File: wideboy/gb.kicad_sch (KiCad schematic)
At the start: 13 parts, among them U12 CPU-AGB, U13 SRAM-AGB, Y1 4.194304M, Y1A 4.194304M

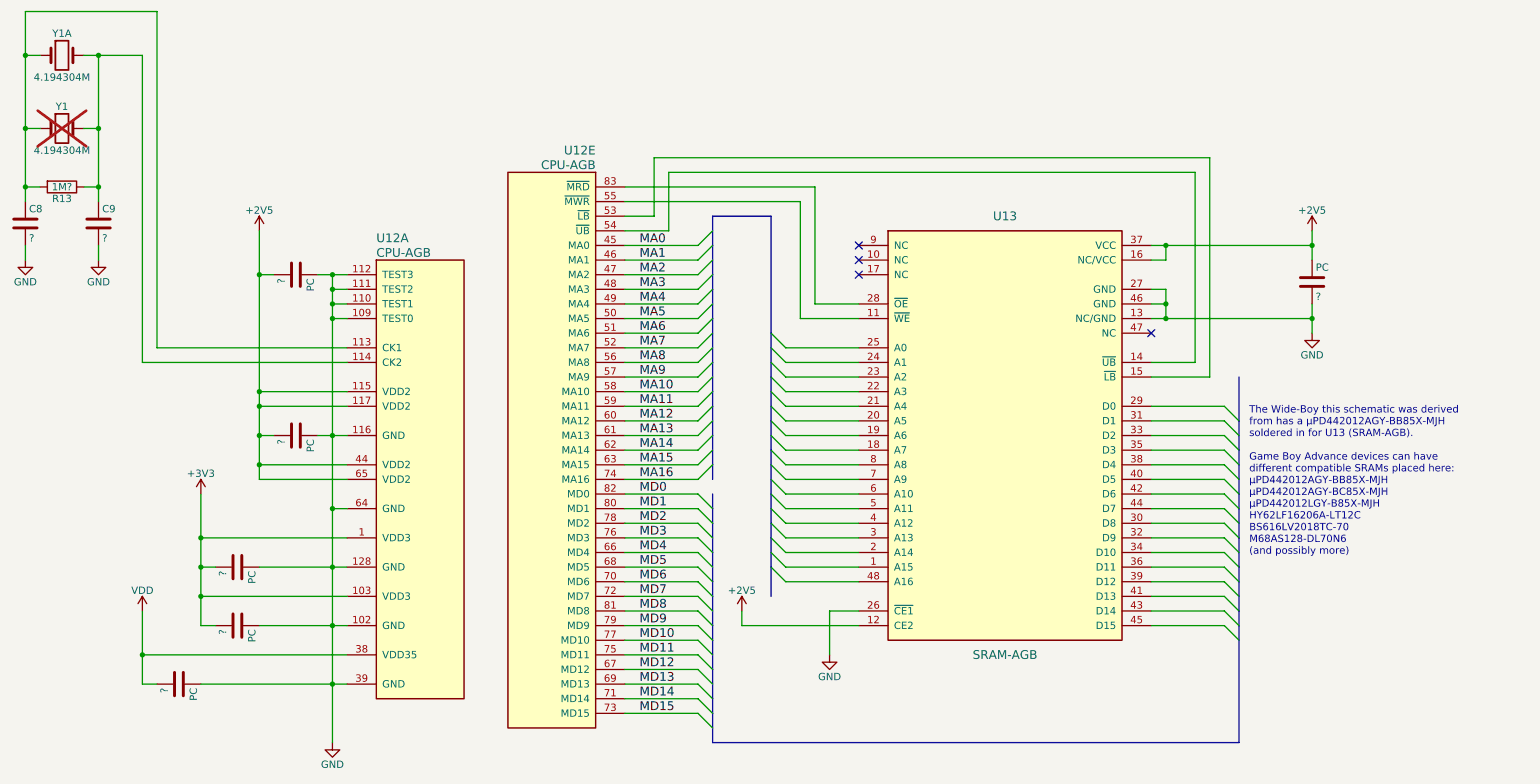
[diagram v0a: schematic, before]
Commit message: Add values for capacitors and diodes
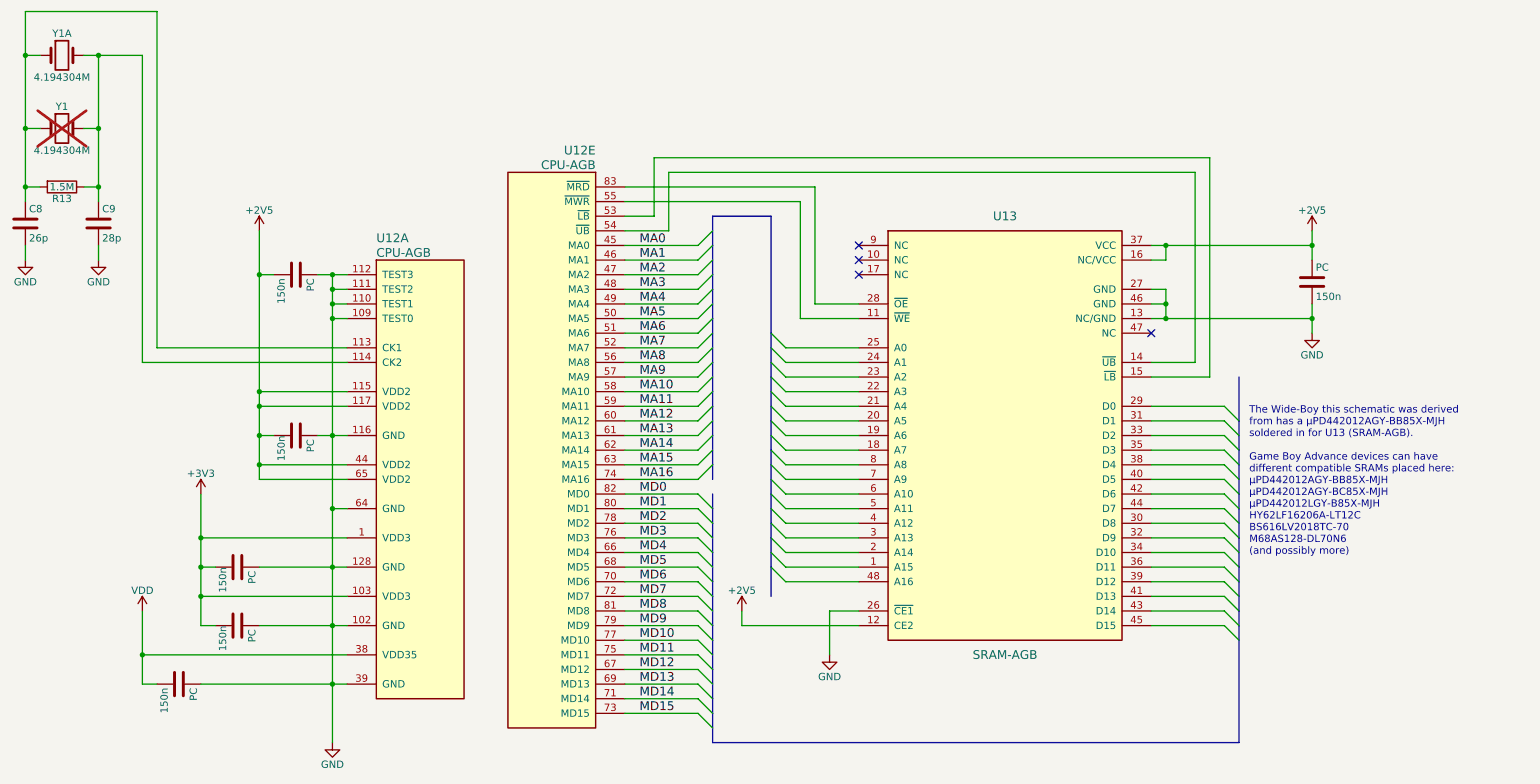
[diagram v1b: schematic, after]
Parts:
- C8: value ? -> 26p
- C9: value ? -> 28p
- PC: value ? -> 150n
- R13: value 1M? -> 1.5M
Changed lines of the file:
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@@
 	(title_block
 		(title "Wide-Boy64 AGB")
-		(date "2024-06-20")
-		(rev "2")
+		(date "2024-09-22")
+		(rev "3")
 		(company "CC-BY-SA-4.0 Michael Singer")
 		(comment 1 "https://github.com/msinger/wideboy/")
@@
 			)
 		)
-		(property "Value" "1M?"
+		(property "Value" "1.5M"
 			(at 34.29 55.88 90)
 			(effects
@@
 			)
 		)
-		(property "Value" "?"
+		(property "Value" "26p"
 			(at 28.575 64.77 0)
 			(effects
@@
 			)
 		)
-		(property "Value" "?"
+		(property "Value" "28p"
 			(at 41.275 64.77 0)
 			(effects
@@
 			)
 		)
-		(property "Value" "?"
+		(property "Value" "150n"
 			(at 72.39 71.755 0)
 			(effects
@@
 			)
 		)
-		(property "Value" "?"
-			(at 72.39 99.695 0)
+		(property "Value" "150n"
+			(at 72.39 99.06 0)
 			(effects
 				(font
@@
 			)
 		)
-		(property "Value" "?"
-			(at 62.23 122.555 0)
+		(property "Value" "150n"
+			(at 62.23 121.92 0)
 			(effects
 				(font
@@
 			)
 		)
-		(property "Value" "?"
-			(at 62.23 132.715 0)
+		(property "Value" "150n"
+			(at 62.23 132.08 0)
 			(effects
 				(font
@@
 			)
 		)
-		(property "Value" "?"
+		(property "Value" "150n"
 			(at 52.07 142.875 0)
 			(effects
@@
 			)
 		)
-		(property "Value" "?"
+		(property "Value" "150n"
 			(at 252.095 74.93 0)
 			(effects
